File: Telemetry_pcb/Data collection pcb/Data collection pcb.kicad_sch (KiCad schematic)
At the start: 0 parts

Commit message: IDK
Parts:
- added 3.3V_RAIL: 3.3, symbol Connector_Generic:Conn_01x15
- added 5V_RAIL: 5V, symbol Connector_Generic:Conn_01x10
- added ADC_MODULE: ADC MODULE, symbol Connector_Generic:Conn_01x10
- added BATTERY_VOLTAGE_DIVIDER (x2): BAT VOLT, symbol Connector_Generic:Conn_01x02
- added ESP32 (x2): Conn_01x18, symbol Connector_Generic:Conn_01x18
- added ESP32 (x2): Conn_01x02, symbol Connector_Generic:Conn_01x02
- added GND_RAIL: GND, symbol Connector_Generic:Conn_01x15
- added GPS: GPS, symbol Connector_Generic:Conn_01x09
- added IMU: IMU, symbol Connector_Generic:Conn_01x08
- added MOTOR_VOLTAGE_DIVIDER (x2): MOT VOLT, symbol Connector_Generic:Conn_01x02
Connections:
- new net 3.3: 3.3V_RAIL.1 (Pin_1), 3.3V_RAIL.10 (Pin_10), 3.3V_RAIL.11 (Pin_11), 3.3V_RAIL.12 (Pin_12), 3.3V_RAIL.13 (Pin_13), 3.3V_RAIL.14 (Pin_14), 3.3V_RAIL.15 (Pin_15), 3.3V_RAIL.2 (Pin_2), 3.3V_RAIL.3 (Pin_3), 3.3V_RAIL.4 (Pin_4), 3.3V_RAIL.5 (Pin_5), 3.3V_RAIL.6 (Pin_6), 3.3V_RAIL.7 (Pin_7), 3.3V_RAIL.8 (Pin_8), 3.3V_RAIL.9 (Pin_9), ESP32.16 (Pin_16), ESP32.17 (Pin_17), GPS.1 (Pin_1), IMU.1 (Pin_1)
- new net 5V: 5V_RAIL.1 (Pin_1), 5V_RAIL.10 (Pin_10), 5V_RAIL.2 (Pin_2), 5V_RAIL.3 (Pin_3), 5V_RAIL.4 (Pin_4), 5V_RAIL.5 (Pin_5), 5V_RAIL.6 (Pin_6), 5V_RAIL.7 (Pin_7), 5V_RAIL.8 (Pin_8), 5V_RAIL.9 (Pin_9), ADC_MODULE.10 (Pin_10), ESP32.2 (Pin_2)
- new net AD0: IMU.7 (Pin_7)
- new net ADDR: ADC_MODULE.6 (Pin_6)
- new net ALERT: ADC_MODULE.5 (Pin_5)
- new net BATGND: BATTERY_VOLTAGE_DIVIDER.1 (Pin_1)
- new net BATPOS: BATTERY_VOLTAGE_DIVIDER.2 (Pin_2)
- new net BATV: ADC_MODULE.4 (Pin_4), BATTERY_VOLTAGE_DIVIDER.2 (Pin_2)
- new net CVOUT: ADC_MODULE.2 (Pin_2)
- new net CVREF: ADC_MODULE.1 (Pin_1)
- new net EN: GPS.2 (Pin_2)
- new net FIX: GPS.4 (Pin_4)
- new net GND: ADC_MODULE.9 (Pin_9), BATTERY_VOLTAGE_DIVIDER.1 (Pin_1), ESP32.1 (Pin_1), ESP32.18 (Pin_18), GND_RAIL.1 (Pin_1), GND_RAIL.10 (Pin_10), GND_RAIL.11 (Pin_11), GND_RAIL.12 (Pin_12), GND_RAIL.13 (Pin_13), GND_RAIL.14 (Pin_14), GND_RAIL.15 (Pin_15), GND_RAIL.2 (Pin_2), GND_RAIL.3 (Pin_3), GND_RAIL.4 (Pin_4), GND_RAIL.5 (Pin_5), GND_RAIL.6 (Pin_6), GND_RAIL.7 (Pin_7), GND_RAIL.8 (Pin_8), GND_RAIL.9 (Pin_9), GPS.7 (Pin_7), IMU.2 (Pin_2), MOTOR_VOLTAGE_DIVIDER.1 (Pin_1)
- new net GP0: ESP32.8 (Pin_8)
- new net GP1: ESP32.7 (Pin_7)
- new net GP15: ESP32.2 (Pin_2)
- new net GP16: ESP32.1 (Pin_1)
- new net GP19: ESP32.18 (Pin_18)
- new net GP2: ESP32.6 (Pin_6)
- new net GP20: ESP32.17 (Pin_17)
- new net GP21: ESP32.16 (Pin_16)
- new net GP26: ESP32.15 (Pin_15)
- new net GP35: ESP32.10 (Pin_10)
- new net GP36: ESP32.9 (Pin_9)
- new net GP37: ESP32.15 (Pin_15)
- new net GP38: ESP32.8 (Pin_8)
- new net GP39: ESP32.9 (Pin_9)
- new net GP40: ESP32.10 (Pin_10)
- new net GP41: ESP32.11 (Pin_11)
- new net GP42: ESP32.12 (Pin_12)
- new net GP43: ESP32.6 (Pin_6)
- new net GP44: ESP32.5 (Pin_5)
- new net GP45: ESP32.13 (Pin_13)
- new net GP46: ESP32.14 (Pin_14)
- new net GP47: ESP32.13 (Pin_13)
- new net GP48: ESP32.14 (Pin_14)
- new net GP5: ESP32.3 (Pin_3)
- new net GP7: ESP32.1 (Pin_1)
- new net GPSRX: ESP32.12 (Pin_12), GPS.6 (Pin_6)
- new net GPSTX: ESP32.11 (Pin_11), GPS.5 (Pin_5)
- new net INT: IMU.8 (Pin_8)
- new net MOTGND: MOTOR_VOLTAGE_DIVIDER.1 (Pin_1)
- new net MOTPOS: MOTOR_VOLTAGE_DIVIDER.2 (Pin_2)
- new net MOTV: ADC_MODULE.3 (Pin_3), MOTOR_VOLTAGE_DIVIDER.2 (Pin_2)
- new net MRPM: ESP32.5 (Pin_5)
- new net PPS: GPS.9 (Pin_9)
- new net RST: ESP32.7 (Pin_7)
- new net SCL: ADC_MODULE.8 (Pin_8), ESP32.1 (Pin_1), IMU.3 (Pin_3)
- new net SDA: ADC_MODULE.7 (Pin_7), ESP32.2 (Pin_2), IMU.4 (Pin_4)
- new net TEMP: ESP32.2 (Pin_2)
- new net VBAT: GPS.3 (Pin_3)
- new net VE: ESP32.3 (Pin_3), ESP32.4 (Pin_4)
- new net VIN: GPS.8 (Pin_8)
- new net WRPM: ESP32.4 (Pin_4)
- new net XCL: IMU.6 (Pin_6)
- new net XDA: IMU.5 (Pin_5)

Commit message: finished schematic need to assign footprints
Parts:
- added BATTERY_VOLTAGE_PADS_1: BATV, symbol Connector_Generic:Conn_01x02
- added CURRENT_SENSOR_PADS_1: CUR, symbol Connector_Generic:Conn_01x04
- added ESC_PADS_1: ESC, symbol Connector_Generic:Conn_01x02
- added MOTOR_VOLTAGE_PADS_1: MOTV, symbol Connector_Generic:Conn_01x02
- added RPM_SENSOR_PADS_1: RPM, symbol Connector_Generic:Conn_01x04
- added SCL_RAIL_1: SCL, symbol Connector_Generic:Conn_01x10
- added SDA_RAIL_1: SDA, symbol Connector_Generic:Conn_01x10
- added SPARE_GPIO_PADS_1: GPIO, symbol Connector_Generic:Conn_01x23
- added TEMP_SENSOR_PADS_1: TEMPS, symbol Connector_Generic:Conn_01x03
- renumbered 3.3V_RAIL to 3.3V_RAIL_1, 5V_RAIL to 5V_RAIL_1, ADC_MODULE to ADC_MODULE_1, BATTERY_VOLTAGE_DIVIDER to BATTERY_VOLTAGE_DIVIDER_1, BATTERY_VOLTAGE_DIVIDER to BATTERY_VOLTAGE_DIVIDER_2, ESP32 to ESP32_1, ESP32 to ESP32_2, ESP32 to ESP32_3, ESP32 to ESP32_4, GND_RAIL to GND_RAIL_1, GPS to GPS_1, IMU to IMU_1, MOTOR_VOLTAGE_DIVIDER to MOTOR_VOLTAGE_DIVIDER_1, MOTOR_VOLTAGE_DIVIDER to MOTOR_VOLTAGE_DIVIDER_2
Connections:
- net 3.3: now also RPM_SENSOR_PADS_1.2 (Pin_2), TEMP_SENSOR_PADS_1.3 (Pin_3)
- net 5V: now also CURRENT_SENSOR_PADS_1.1 (Pin_1)
- net BATGND: now also BATTERY_VOLTAGE_PADS_1.1 (Pin_1)
- net BATPOS: now also BATTERY_VOLTAGE_PADS_1.2 (Pin_2)
- net CVOUT: now also CURRENT_SENSOR_PADS_1.3 (Pin_3)
- net CVREF: now also CURRENT_SENSOR_PADS_1.4 (Pin_4)
- net GND: now also CURRENT_SENSOR_PADS_1.2 (Pin_2), RPM_SENSOR_PADS_1.1 (Pin_1), TEMP_SENSOR_PADS_1.1 (Pin_1)
- net GP0: now also SPARE_GPIO_PADS_1.21 (Pin_21)
- net GP1: now also SPARE_GPIO_PADS_1.4 (Pin_4)
- net GP15: now also SPARE_GPIO_PADS_1.22 (Pin_22)
- net GP16: now also SPARE_GPIO_PADS_1.23 (Pin_23)
- net GP19: now also SPARE_GPIO_PADS_1.13 (Pin_13)
- net GP2: now also SPARE_GPIO_PADS_1.3 (Pin_3)
- net GP20: now also SPARE_GPIO_PADS_1.14 (Pin_14)
- net GP21: now also SPARE_GPIO_PADS_1.15 (Pin_15)
- net GP26: now also SPARE_GPIO_PADS_1.16 (Pin_16)
- net GP35: now also SPARE_GPIO_PADS_1.19 (Pin_19)
- net GP36: now also SPARE_GPIO_PADS_1.20 (Pin_20)
- net GP37: now also SPARE_GPIO_PADS_1.12 (Pin_12)
- net GP38: now also SPARE_GPIO_PADS_1.5 (Pin_5)
- net GP39: now also SPARE_GPIO_PADS_1.6 (Pin_6)
- net GP40: now also SPARE_GPIO_PADS_1.7 (Pin_7)
- net GP41: now also SPARE_GPIO_PADS_1.8 (Pin_8)
- net GP42: now also SPARE_GPIO_PADS_1.9 (Pin_9)
- net GP45: now also SPARE_GPIO_PADS_1.10 (Pin_10)
- net GP46: now also SPARE_GPIO_PADS_1.11 (Pin_11)
- net GP47: now also SPARE_GPIO_PADS_1.18 (Pin_18)
- net GP48: now also SPARE_GPIO_PADS_1.17 (Pin_17)
- net GP5: now also SPARE_GPIO_PADS_1.2 (Pin_2)
- net GP7: now also SPARE_GPIO_PADS_1.1 (Pin_1)
- net MOTGND: now also MOTOR_VOLTAGE_PADS_1.1 (Pin_1)
- net MOTPOS: now also MOTOR_VOLTAGE_PADS_1.2 (Pin_2)
- net MRPM: now also RPM_SENSOR_PADS_1.4 (Pin_4)
- net SCL: now also SCL_RAIL_1.1 (Pin_1), SCL_RAIL_1.10 (Pin_10), SCL_RAIL_1.2 (Pin_2), SCL_RAIL_1.3 (Pin_3), SCL_RAIL_1.4 (Pin_4), SCL_RAIL_1.5 (Pin_5), SCL_RAIL_1.6 (Pin_6), SCL_RAIL_1.7 (Pin_7), SCL_RAIL_1.8 (Pin_8), SCL_RAIL_1.9 (Pin_9)
- net SDA: now also SDA_RAIL_1.1 (Pin_1), SDA_RAIL_1.10 (Pin_10), SDA_RAIL_1.2 (Pin_2), SDA_RAIL_1.3 (Pin_3), SDA_RAIL_1.4 (Pin_4), SDA_RAIL_1.5 (Pin_5), SDA_RAIL_1.6 (Pin_6), SDA_RAIL_1.7 (Pin_7), SDA_RAIL_1.8 (Pin_8), SDA_RAIL_1.9 (Pin_9)
- net TEMP: now also TEMP_SENSOR_PADS_1.2 (Pin_2)
- net WRPM: now also RPM_SENSOR_PADS_1.3 (Pin_3)
- net GP43 renamed ESC_RX
- net ESC_RX: now also ESC_PADS_1.1 (Pin_1)
- net GP44 renamed ESC_TX
- net ESC_TX: now also ESC_PADS_1.2 (Pin_2)

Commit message: finished layout
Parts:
- removed ADC_MODULE_1: ADC MODULE, symbol Connector_Generic:Conn_01x10
- removed BATTERY_VOLTAGE_DIVIDER_1, BATTERY_VOLTAGE_DIVIDER_2: BAT VOLT, symbol Connector_Generic:Conn_01x02
- removed ESP32_1, ESP32_4: Conn_01x18, symbol Connector_Generic:Conn_01x18
- removed ESP32_2, ESP32_3: Conn_01x02, symbol Connector_Generic:Conn_01x02
- removed GPS_1: GPS, symbol Connector_Generic:Conn_01x09
- removed IMU_1: IMU, symbol Connector_Generic:Conn_01x08
- removed MOTOR_VOLTAGE_DIVIDER_1, MOTOR_VOLTAGE_DIVIDER_2: MOT VOLT, symbol Connector_Generic:Conn_01x02
- added U1: HELTEC V4 LORA, greenpower telemetry footprints:HELTEC V4, symbol greenpower telemetry library:Heltec_V4
- added U2: ADC_MODULE, greenpower telemetry footprints:ADC_MODULE, symbol greenpower telemetry library:ADC_MODULE
- added U3: ACCELEROMETER, greenpower telemetry footprints:ACCELEROMETER, symbol greenpower telemetry library:ACCELEROMETER
- added U4: GPS_MODULE, greenpower telemetry footprints:GPS_MODULE, symbol greenpower telemetry library:GPS_MODULE
- added U5, U6: VOLTAGE_DIVIDER, greenpower telemetry footprints:VOLTAGE_DIVIDER, symbol greenpower telemetry library:VOLTAGE_DIVIDER
- 3.3V_RAIL_1, GND_RAIL_1: footprint (none) -> greenpower telemetry footprints:1X15 PADS
- 5V_RAIL_1, SCL_RAIL_1, SDA_RAIL_1: footprint (none) -> greenpower telemetry footprints:1X10 PADS
- BATTERY_VOLTAGE_PADS_1, ESC_PADS_1, MOTOR_VOLTAGE_PADS_1: footprint (none) -> greenpower telemetry footprints:1X02 PADS
- CURRENT_SENSOR_PADS_1, RPM_SENSOR_PADS_1: footprint (none) -> greenpower telemetry footprints:1X04 PADS
- SPARE_GPIO_PADS_1: footprint (none) -> greenpower telemetry footprints:1X23 PADS
- TEMP_SENSOR_PADS_1: footprint (none) -> greenpower telemetry footprints:1X03 PADS
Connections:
- net 3.3: now also U1.16 (3V3), U1.17 (3V3), U3.1 (VCC), U4.1 (3.3)
- net 5V: now also U1.20 (5V), U2.10 (VCC)
- net AD0: now also U3.7 (AD0)
- net ADDR: now also U2.6 (ADDR)
- net ALERT: now also U2.5 (ALERT)
- net BATGND: now also U5.1 (-IN)
- net BATPOS: now also U5.2 (+IN)
- net BATV: now also U2.4 (A0), U5.3 (+OUT)
- net CVOUT: now also U2.2 (A2)
- net CVREF: now also U2.1 (A3)
- net EN: now also U4.2 (EN)
- net ESC_RX: now also U1.24 (GPIO43)
- net ESC_TX: now also U1.23 (GPIO44)
- net FIX: now also U4.4 (FIX)
- net GND: now also U1.18 (GND), U1.19 (GND), U2.9 (GND), U3.2 (GND), U4.7 (GND), U5.4 (-OUT), U6.4 (-OUT)
- net GP0: now also U1.26 (GPIO0)
- net GP1: now also U1.7 (GPIO1)
- net GP15: now also U1.40 (GPIO15)
- net GP16: now also U1.39 (GPIO16)
- net GP19: now also U1.36 (GPIO19)
- net GP2: now also U1.6 (GPIO2)
- net GP20: now also U1.35 (GPIO20)
- net GP21: now also U1.34 (GPIO21)
- net GP26: now also U1.33 (GPIO26)
- net GP35: now also U1.28 (GPIO35)
- net GP36: now also U1.27 (GPIO36)
- net GP37: now also U1.15 (GPIO37)
- net GP38: now also U1.8 (GPIO38)
- net GP39: now also U1.9 (GPIO39)
- net GP40: now also U1.10 (GPIO40)
- net GP41: now also U1.11 (GPIO41)
- net GP42: now also U1.12 (GPIO42)
- net GP45: now also U1.13 (GPIO45)
- net GP46: now also U1.14 (GPIO46)
- net GP47: now also U1.31 (GPIO47)
- net GP48: now also U1.32 (GPIO48)
- net GP5: now also U1.3 (GPIO5)
- net GP7: now also U1.1 (GPIO7)
- net GPSRX: now also U1.30 (GPIO33), U4.6 (RX)
- net GPSTX: now also U1.29 (GPIO34), U4.5 (TX)
- net INT: now also U3.8 (INT)
- net MOTGND: now also U6.1 (-IN)
- net MOTPOS: now also U6.2 (+IN)
- net MOTV: now also U2.3 (A1), U6.3 (+OUT)
- net MRPM: now also U1.5 (GPIO3)
- net PPS: now also U4.9 (PPS)
- net RST: now also U1.25 (RST)
- net SCL: now also U1.37 (GPIO18), U2.8 (SCL), U3.3 (SCL)
- net SDA: now also U1.38 (GPIO17), U2.7 (SDA), U3.4 (SDA)
- net TEMP: now also U1.2 (GPIO6)
- net VBAT: now also U4.3 (VBAT)
- net VE: now also U1.21 (VE), U1.22 (VE)
- net VIN: now also U4.8 (VIN)
- net WRPM: now also U1.4 (GPIO4)
- net XCL: now also U3.6 (XCL)
- net XDA: now also U3.5 (XDA)
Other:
- moved on the sheet: 5V_RAIL_1, BATTERY_VOLTAGE_PADS_1, CURRENT_SENSOR_PADS_1, ESC_PADS_1, MOTOR_VOLTAGE_PADS_1, RPM_SENSOR_PADS_1, SCL_RAIL_1, SDA_RAIL_1, TEMP_SENSOR_PADS_1

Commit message: idkidkidkidkidkidk
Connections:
- net 3.3 renamed +3.3V
- net 5V renamed +5V

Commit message: finished data collection pcb
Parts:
- added H1, H2, H3, H4: MountingHole, MountingHole:MountingHole_3.2mm_M3, symbol Mechanical:MountingHole

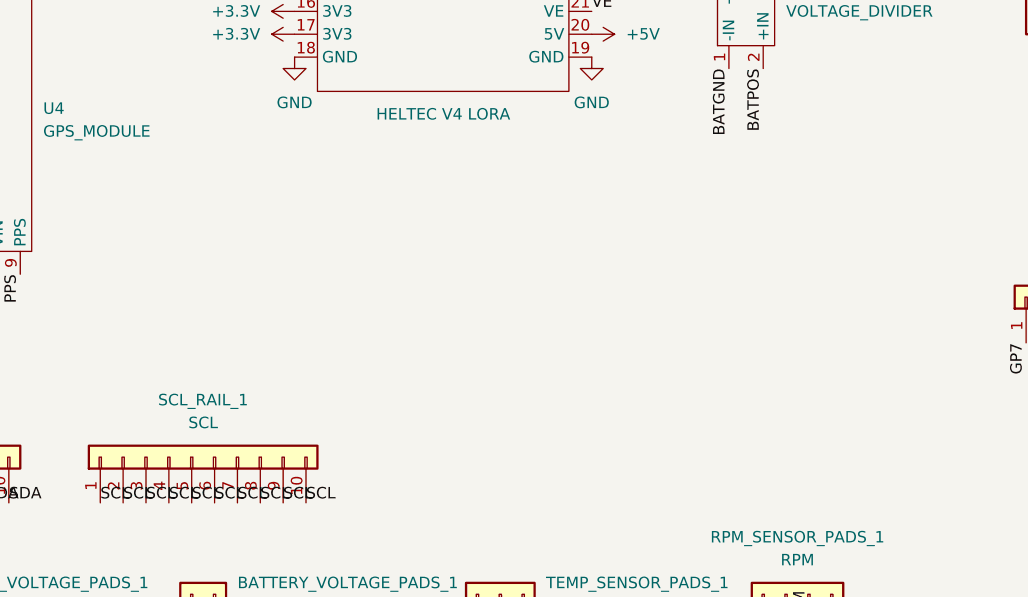
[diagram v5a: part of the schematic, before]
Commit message: added sd and rtc to pcb
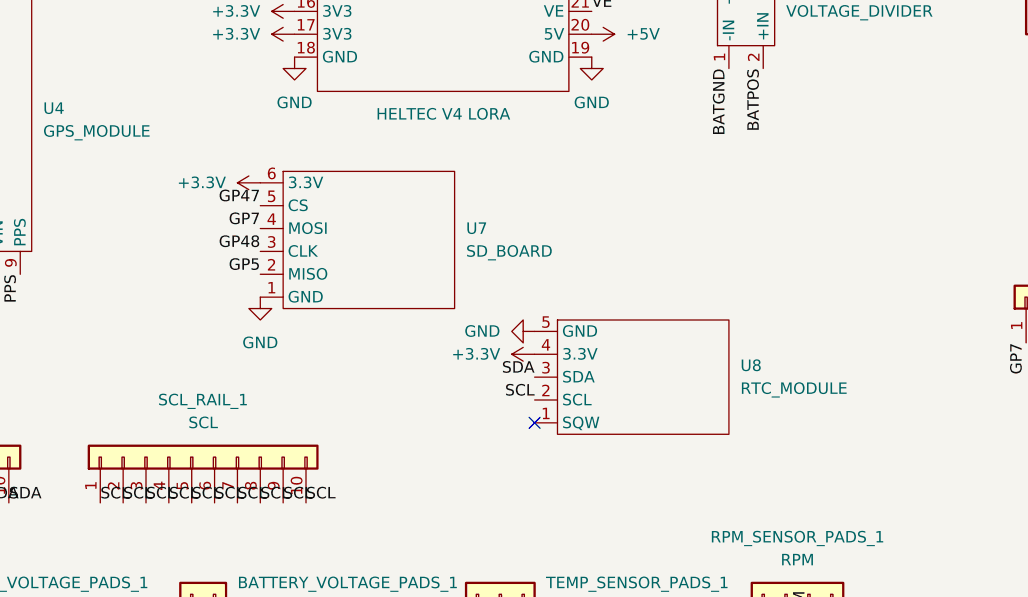
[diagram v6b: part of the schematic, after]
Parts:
- added U7: SD_BOARD, telem_system_footprint_library:SD_BOARD, symbol telem_system_symbol_library:SD_CARD_BOARD
- added U8: RTC_MODULE, telem_system_footprint_library:RTC_MODULE, symbol telem_system_symbol_library:RTC_MODULE
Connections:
- net +3.3V: now also U7.6 (3.3V), U8.4 (3.3V)
- net GND: now also U7.1 (GND), U8.5 (GND)
- net GP47: now also U7.5 (CS)
- net GP48: now also U7.3 (CLK)
- net GP5: now also U7.2 (MISO)
- net GP7: now also U7.4 (MOSI)
- net SCL: now also U8.2 (SCL)
- net SDA: now also U8.3 (SDA)
- no-connect marks 0 -> 1
